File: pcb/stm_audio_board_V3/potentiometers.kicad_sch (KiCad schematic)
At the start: 0 parts

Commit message: nothing
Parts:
- added RV1, RV2, RV3, RV4, RV5, RV6: R_Potentiometer, Potentiometer_THT:Potentiometer_Piher_T-16L_Single_Vertical_Hole, symbol Device:R_Potentiometer
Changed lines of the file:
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@@
 (kicad_sch (version 20230121) (generator eeschema)
   (paper "A4")
+  (symbol (lib_id "Device:R_Potentiometer") (at 46.99 58.42 0) (unit 1)
+    (in_bom yes) (on_board yes) (dnp no) (fields_autoplaced)
+    (property "Reference" "RV4" (at 44.45 57.785 0)
+      (effects (font (size 1.27 1.27)) (justify right))
+    )
+    (property "Value" "R_Potentiometer" (at 44.45 60.325 0)
+      (effects (font (size 1.27 1.27)) (justify right))
+    )
+    (property "Footprint" "Potentiometer_THT:Potentiometer_Piher_T-16L_Single_Vertical_Hole" (at 46.99 58.42 0)
+      (effects (font (size 1.27 1.27)) hide)
+    )
+    (property "Datasheet" "~" (at 46.99 58.42 0)
+      (effects (font (size 1.27 1.27)) hide)
+    )
+    (pin "1")
+    (pin "2")
+    (pin "3")
+    (instances
+      (project "stm_audio_board_V3"
+        (path "/6997cf63-2615-4e49-9471-e7da1b6bae71/f3a016e9-328b-49a9-9257-9482800e0ff5"
+          (reference "RV4") (unit 1)
+        )
+      )
+    )
+  )
+  (symbol (lib_id "Device:R_Potentiometer") (at 69.85 48.26 0) (unit 1)
+    (in_bom yes) (on_board yes) (dnp no) (fields_autoplaced)
+    (property "Reference" "RV2" (at 67.31 47.625 0)
+      (effects (font (size 1.27 1.27)) (justify right))
+    )
+    (property "Value" "R_Potentiometer" (at 67.31 50.165 0)
+      (effects (font (size 1.27 1.27)) (justify right))
+    )
+    (property "Footprint" "Potentiometer_THT:Potentiometer_Piher_T-16L_Single_Vertical_Hole" (at 69.85 48.26 0)
+      (effects (font (size 1.27 1.27)) hide)
+    )
+    (property "Datasheet" "~" (at 69.85 48.26 0)
+      (effects (font (size 1.27 1.27)) hide)
+    )
+    (pin "1")
+    (pin "2")
+    (pin "3")
+    (instances
+      (project "stm_audio_board_V3"
+        (path "/6997cf63-2615-4e49-9471-e7da1b6bae71/f3a016e9-328b-49a9-9257-9482800e0ff5"
+          (reference "RV2") (unit 1)
+        )
+      )
+    )
+  )
+  (symbol (lib_id "Device:R_Potentiometer") (at 69.85 58.42 0) (unit 1)
+    (in_bom yes) (on_board yes) (dnp no) (fields_autoplaced)
+    (property "Reference" "RV5" (at 67.31 57.785 0)
+      (effects (font (size 1.27 1.27)) (justify right))
+    )
+    (property "Value" "R_Potentiometer" (at 67.31 60.325 0)
+      (effects (font (size 1.27 1.27)) (justify right))
+    )
+    (property "Footprint" "Potentiometer_THT:Potentiometer_Piher_T-16L_Single_Vertical_Hole" (at 69.85 58.42 0)
+      (effects (font (size 1.27 1.27)) hide)
+    )
+    (property "Datasheet" "~" (at 69.85 58.42 0)
+      (effects (font (size 1.27 1.27)) hide)
+    )
+    (pin "1")
+    (pin "2")
+    (pin "3")
+    (instances
+      (project "stm_audio_board_V3"
+        (path "/6997cf63-2615-4e49-9471-e7da1b6bae71/f3a016e9-328b-49a9-9257-9482800e0ff5"
+          (reference "RV5") (unit 1)
+        )
+      )
+    )
+  )
+  (symbol (lib_id "Device:R_Potentiometer") (at 46.99 48.26 0) (unit 1)
+    (in_bom yes) (on_board yes) (dnp no) (fields_autoplaced)
+    (property "Reference" "RV1" (at 44.45 47.625 0)
+      (effects (font (size 1.27 1.27)) (justify right))
+    )
+    (property "Value" "R_Potentiometer" (at 44.45 50.165 0)
+      (effects (font (size 1.27 1.27)) (justify right))
+    )
+    (property "Footprint" "Potentiometer_THT:Potentiometer_Piher_T-16L_Single_Vertical_Hole" (at 46.99 48.26 0)
+      (effects (font (size 1.27 1.27)) hide)
+    )
+    (property "Datasheet" "~" (at 46.99 48.26 0)
+      (effects (font (size 1.27 1.27)) hide)
+    )
+    (pin "1")
+    (pin "2")
+    (pin "3")
+    (instances
+      (project "stm_audio_board_V3"
+        (path "/6997cf63-2615-4e49-9471-e7da1b6bae71/f3a016e9-328b-49a9-9257-9482800e0ff5"
+          (reference "RV1") (unit 1)
+        )
+      )
+    )
+  )
+  (symbol (lib_id "Device:R_Potentiometer") (at 92.71 48.26 0) (unit 1)
+    (in_bom yes) (on_board yes) (dnp no) (fields_autoplaced)
+    (property "Reference" "RV3" (at 90.17 47.625 0)
+      (effects (font (size 1.27 1.27)) (justify right))
+    )
+    (property "Value" "R_Potentiometer" (at 90.17 50.165 0)
+      (effects (font (size 1.27 1.27)) (justify right))
+    )
+    (property "Footprint" "Potentiometer_THT:Potentiometer_Piher_T-16L_Single_Vertical_Hole" (at 92.71 48.26 0)
+      (effects (font (size 1.27 1.27)) hide)
+    )
+    (property "Datasheet" "~" (at 92.71 48.26 0)
+      (effects (font (size 1.27 1.27)) hide)
+    )
+    (pin "1")
+    (pin "2")
+    (pin "3")
+    (instances
+      (project "stm_audio_board_V3"
+        (path "/6997cf63-2615-4e49-9471-e7da1b6bae71/f3a016e9-328b-49a9-9257-9482800e0ff5"
+          (reference "RV3") (unit 1)
+        )
+      )
+    )
+  )
+  (symbol (lib_id "Device:R_Potentiometer") (at 92.71 58.42 0) (unit 1)
+    (in_bom yes) (on_board yes) (dnp no) (fields_autoplaced)
+    (property "Reference" "RV6" (at 90.17 57.785 0)
+      (effects (font (size 1.27 1.27)) (justify right))
+    )
+    (property "Value" "R_Potentiometer" (at 90.17 60.325 0)
+      (effects (font (size 1.27 1.27)) (justify right))
+    )
+    (property "Footprint" "Potentiometer_THT:Potentiometer_Piher_T-16L_Single_Vertical_Hole" (at 92.71 58.42 0)
+      (effects (font (size 1.27 1.27)) hide)
+    )
+    (property "Datasheet" "~" (at 92.71 58.42 0)
+      (effects (font (size 1.27 1.27)) hide)
+    )
+    (pin "1")
+    (pin "2")
+    (pin "3")
+    (instances
+      (project "stm_audio_board_V3"
+        (path "/6997cf63-2615-4e49-9471-e7da1b6bae71/f3a016e9-328b-49a9-9257-9482800e0ff5"
+          (reference "RV6") (unit 1)
+        )
+      )
+    )
+  )
 )

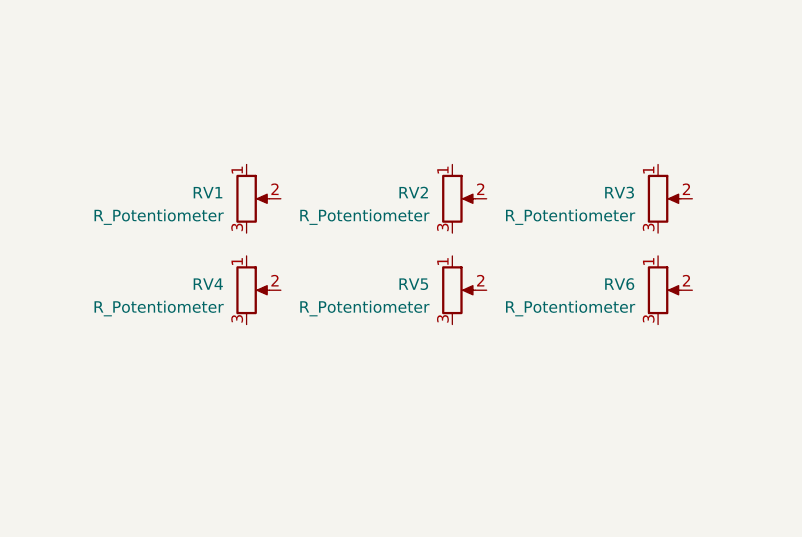
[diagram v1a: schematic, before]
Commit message: potmeter for V3 changed
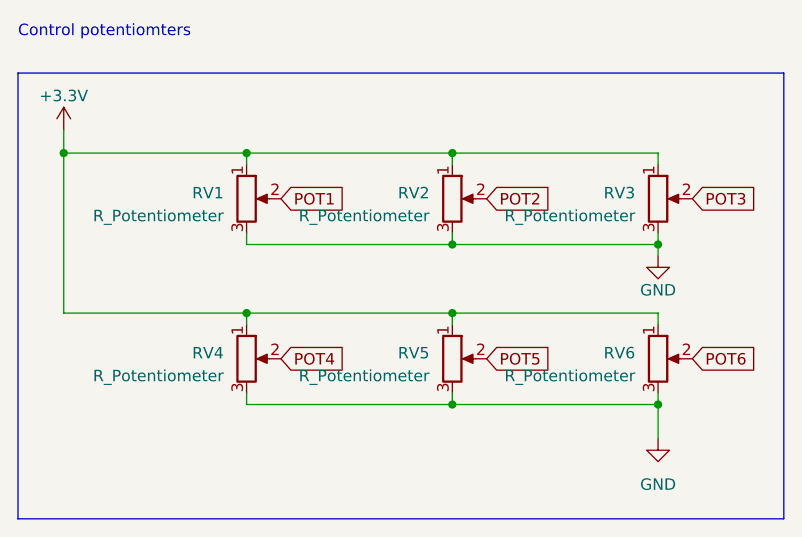
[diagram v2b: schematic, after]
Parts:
- RV1, RV2, RV3, RV4, RV5, RV6: footprint Potentiometer_THT:Potentiometer_Piher_T-16L_Single_Vertical_Hole -> Potentiometer_THT:Potentiometer_Omeg_PC16BU_Vertical
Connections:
- net +3.3V: now reaches RV4.1
- net +3.3V: now also RV1.1, RV2.1, RV3.1, RV5.1, RV6.1
- net POT4: now reaches RV4.2
- net GND: now reaches RV4.3
- net GND: now also RV1.3, RV2.3, RV3.3, RV5.3, RV6.3
- net POT2: now reaches RV2.2
- net POT5: now reaches RV5.2
- net POT1: now reaches RV1.2
- net POT3: now reaches RV3.2
- net POT6: now reaches RV6.2
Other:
- note added: "Control potentiomters"
- moved on the sheet: RV4, RV5, RV6
